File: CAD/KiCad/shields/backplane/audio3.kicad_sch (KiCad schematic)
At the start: 4 parts

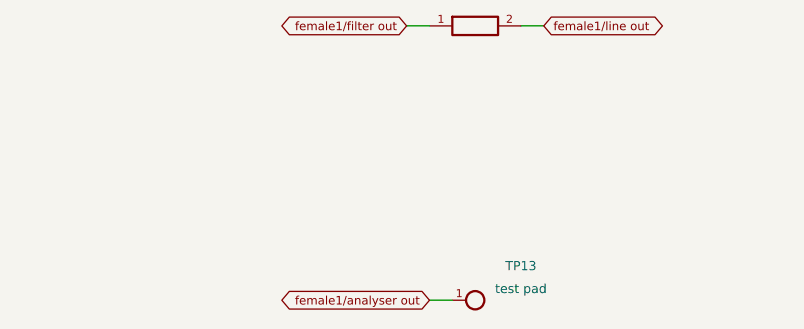
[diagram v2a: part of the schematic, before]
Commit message: Update shields for Thomas RC cards, debug headers and body microphones
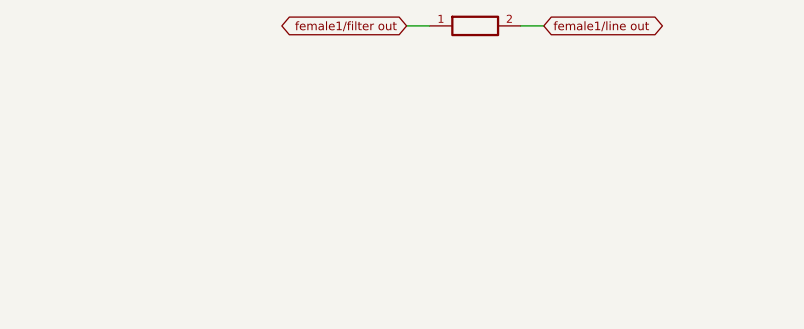
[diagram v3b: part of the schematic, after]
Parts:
- removed TP13: test pad, Shields:TestPoint_Pad_D1.5mm, symbol Colloquy:TP13
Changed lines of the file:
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@@
 (wire (pts (xy 330.2000 50.8000) (xy 332.7400 50.8000)) (stroke (width 0) (type default)))
 (global_label "AGND" (shape bidirectional) (at 332.7400 50.8000 0) (effects (font (size 0.95 0.95)) (justify left)) (property "Intersheetrefs" "${INTERSHEET_REFS}" (at 332.7400 50.8000 0) (effects (font (size 1.016 1.016))  (hide yes))))
-(symbol (lib_id "Colloquy:TP13") (at 66.0400 81.2800 0) (unit 1) (exclude_from_sim no) (in_bom no) (on_board yes) (dnp no)
-(property "Reference" "TP13" (at 71.1200 77.4700 0) (effects (font (size 1.016 1.016))  ))
-(property "Value" "test pad" (at 71.1200 80.0100 0) (effects (font (size 1.016 1.016))  ))
-(property "Footprint" "Shields:TestPoint_Pad_D1.5mm" (at 66.0400 81.2800 0) (effects (font (size 1.27 1.27))  (hide yes)))
-(property "Datasheet" "" (at 66.0400 81.2800 0) (effects (font (size 1.27 1.27))  (hide yes)))
-(property "Description" "female1 analyser output, module 0" (at 66.0400 81.2800 0) (effects (font (size 1.27 1.27))  (hide yes)))
-(pin "1")
-(instances (project "backplane" (path "/c974ff16-a701-53ef-8165-966482bbbbae/905df8d0-f9b6-5ac9-b63e-bb1b87483a24" (reference "TP13") (unit 1)))))
-(wire (pts (xy 63.5000 81.2800) (xy 60.9600 81.2800)) (stroke (width 0) (type default)))
-(global_label "female1/analyser out" (shape bidirectional) (at 60.9600 81.2800 180) (effects (font (size 0.95 0.95)) (justify right)) (property "Intersheetrefs" "${INTERSHEET_REFS}" (at 60.9600 81.2800 0) (effects (font (size 1.016 1.016))  (hide yes))))
           (embedded_fonts no))
